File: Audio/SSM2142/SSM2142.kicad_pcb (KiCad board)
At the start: 2 copper layers, 50.8 x 64.8 mm, 11 parts, among them P1 CONN_01X03, P2 CONN_01X02, P3 CONN_01X02, P4 CONN_01X02, U1 SSM2142P

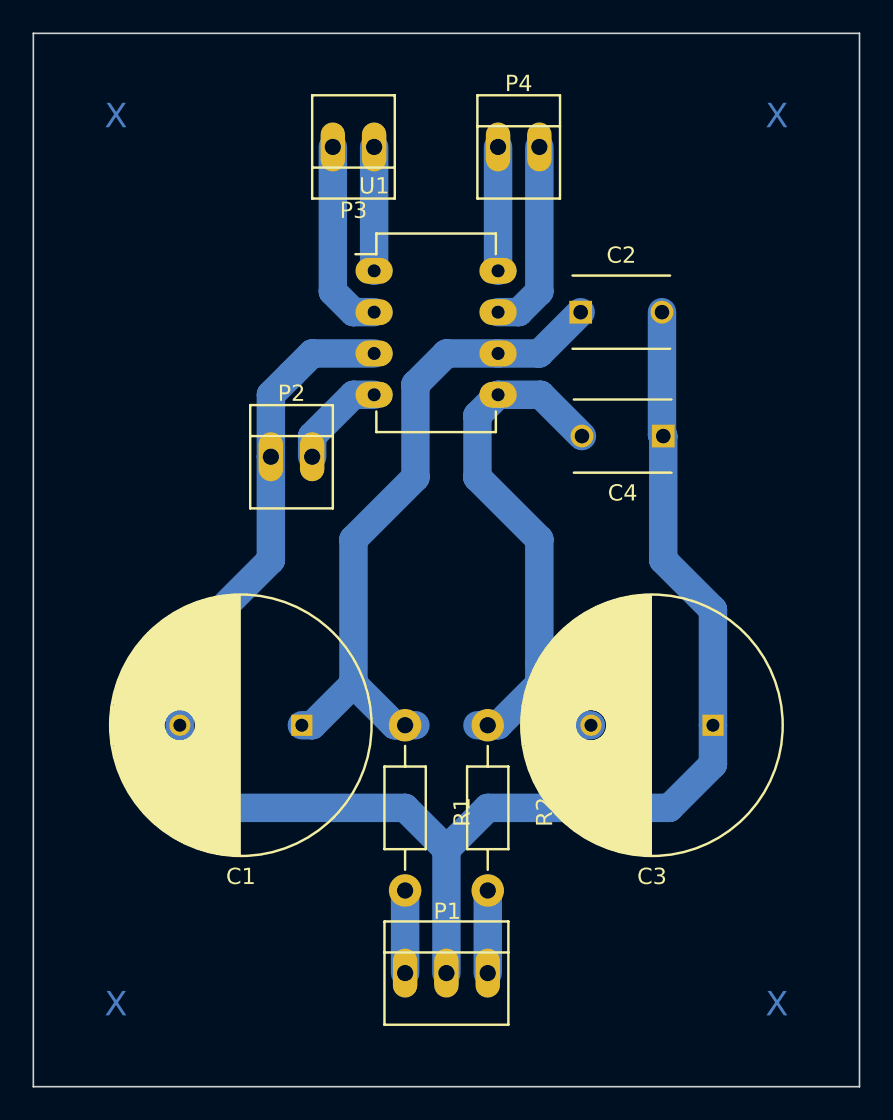
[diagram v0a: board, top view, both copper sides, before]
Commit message: Fixes for SSM2142(PCB)
Reworked for smaller footprint of PCB.
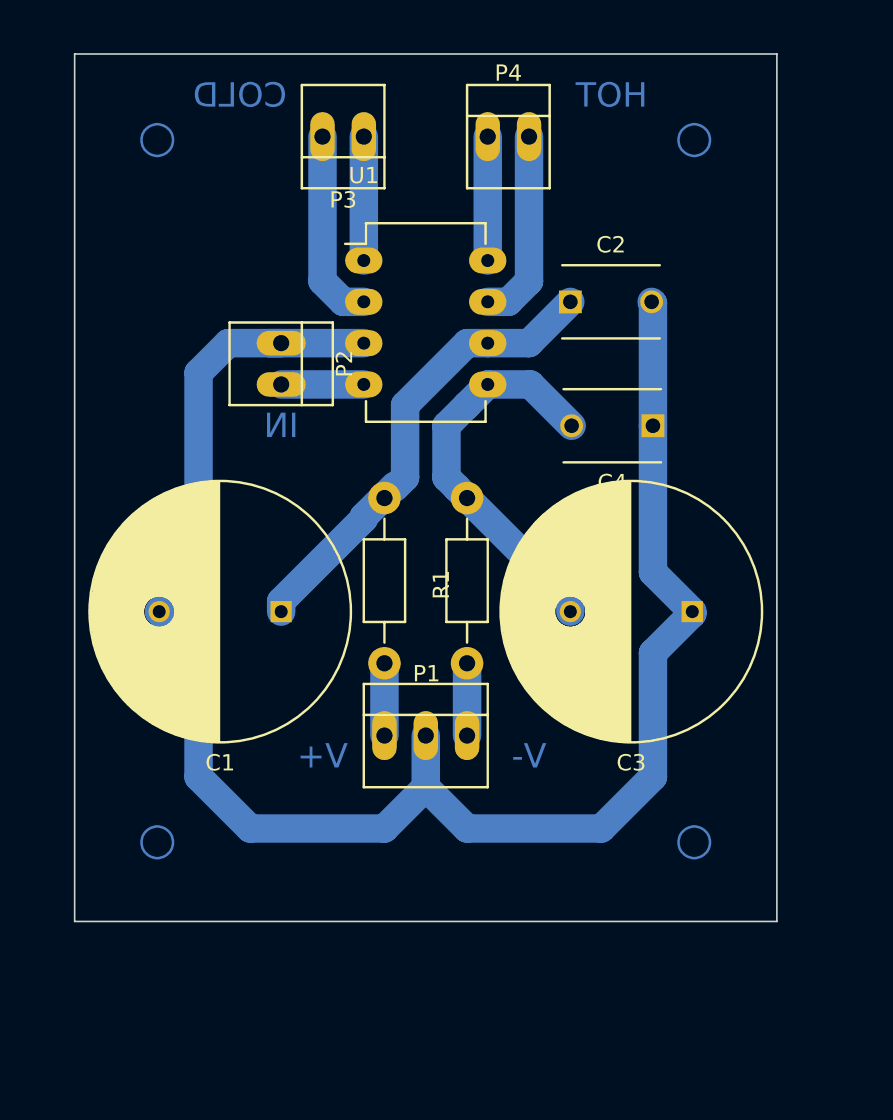
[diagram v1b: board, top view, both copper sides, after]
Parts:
- moved P1 14.7 mm to (102.9, 82.5)
- moved R1 14.0 mm to (100.3, 73.0)
- moved R2 14.0 mm to (105.4, 73.0)
- moved C1 7.10 mm to (94.0, 74.9)
- moved C3 7.10 mm to (119.3, 74.9)
- moved P2 5.75 mm to (94.0, 59.7), turned to 270 degrees
- moved C4 0.90 mm to (116.8, 63.5)
- moved C2 0.90 mm to (111.8, 55.9)
- moved P3 0.90 mm to (97.8, 45.7)
- moved P4 0.90 mm to (108.0, 45.7)
- moved U1 0.90 mm to (99.1, 53.3)
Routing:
- net +V_L: track 41.1 -> 28.8 mm
- net -V_L: track 35.2 -> 24.4 mm
- net Vin_L: track 6.13 -> 5.08 mm
- net GND: track 106.4 -> 105.7 mm
- net -Vreg: track 5.08 -> 4.44 mm
- net +Vreg: track 5.08 -> 4.44 mm
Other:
- board size 50.8 x 64.8 mm -> 43.2 x 53.3 mm
- board text added: "COLD"
- board text added: "HOT"
- board text added: "IN"
- board text added: "V+"
- board text added: "V-"
- board text added: "○"
- board text removed: "X"
